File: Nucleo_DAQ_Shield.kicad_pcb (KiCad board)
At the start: 2 copper layers, 53.3 x 78.1 mm, 35 parts, among them J1 CONN_01X06, J2 CONN_01X06, J3 CONN_01X02, J4 CONN_01X02, J6 CONN_COAXIAL, J7 CONN_01X02, U1 4050, U10 ST_Nucleo144_F746ZG_CN10, U2 TL072, U3 LM7805CT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

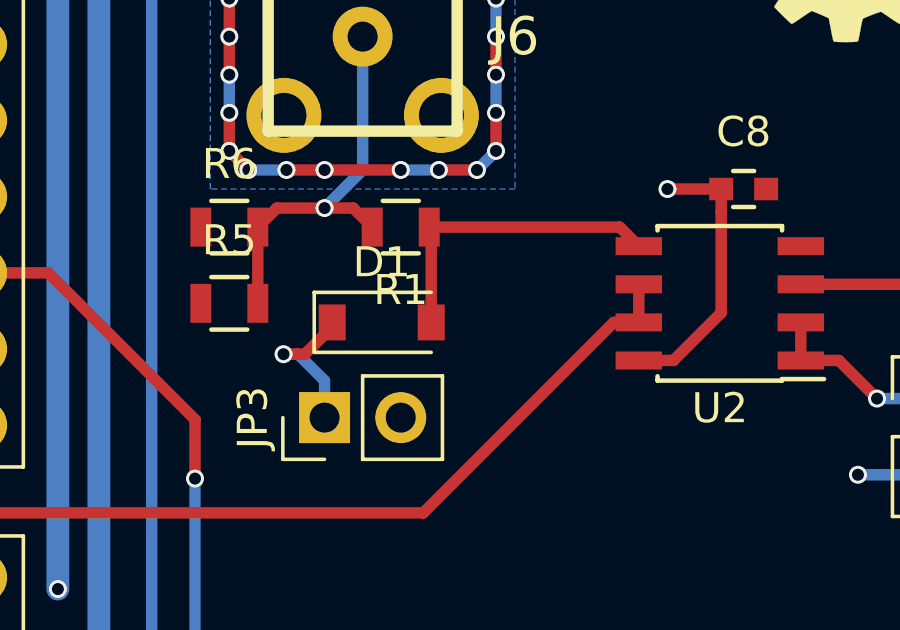
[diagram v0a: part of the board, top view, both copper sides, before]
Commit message: Added through hold Schottky diode as an alternative to SOD-123 Schottky diode
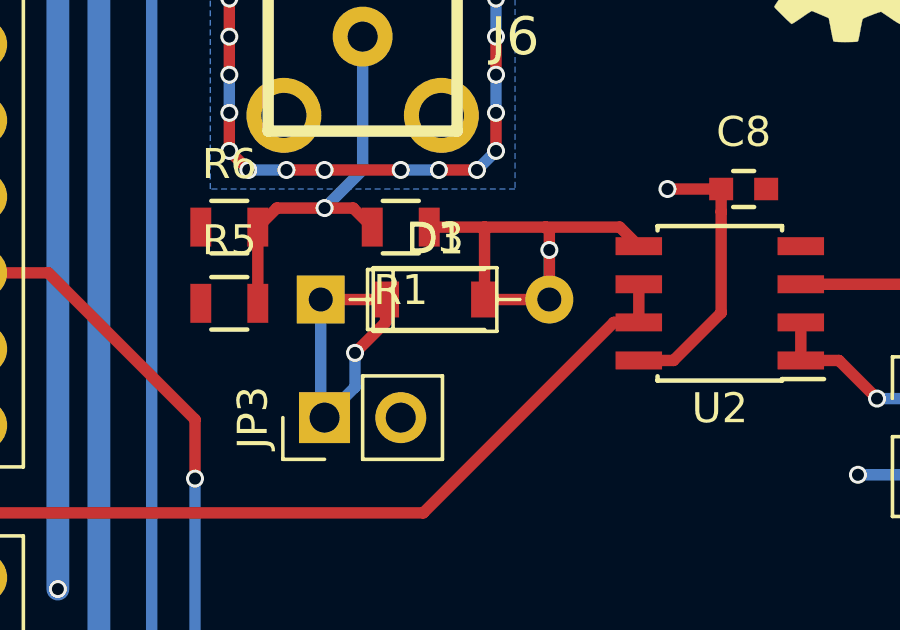
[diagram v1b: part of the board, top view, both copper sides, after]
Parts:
- added D3: SD103 DO-35, Diodes_THT:D_DO-35_SOD27_P7.62mm_Horizontal, F.Cu at (157.4, 79.9)
- D1: value D_Schottky -> SD103 SOD-123
- moved D1 1.94 mm to (161.2, 79.9)
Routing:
- net Net-(D1-Pad1): track 5.11 -> 10.9 mm
- net /ENVLP: track 10.4 -> 16.0 mm, vias 0 -> 1
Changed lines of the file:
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@@
 (kicad_pcb (version 4) (host pcbnew 4.0.6)
   (general
-    (links 0)
+    (links 79)
     (no_connects 2)
-    (area 140.894999 48.819999 194.385001 127.075001)
+    (area 133.708523 46.841 244.462898 140.391001)
     (thickness 1.6)
     (drawings 22)
-    (tracks 292)
+    (tracks 299)
     (zones 0)
-    (modules 35)
+    (modules 36)
     (nets 112)
   )
@@
     (visible_elements FFFFEF7F)
     (pcbplotparams
-      (layerselection 0x00030_80000001)
+      (layerselection 0x01000_80000001)
       (usegerberextensions false)
       (excludeedgelayer true)
@@
       (outputformat 1)
       (mirror false)
-      (drillshape 1)
+      (drillshape 0)
       (scaleselection 1)
-      (outputdirectory ""))
+      (outputdirectory gerbers/v1.0/))
   )
   (net 0 "")
@@
   )
   (module Diodes_SMD:D_SOD-123 (layer F.Cu)
-    (at 159.385 80.645)
+    (at 161.164 79.883)
     (descr SOD-123)
     (tags SOD-123)
@@
       (effects (font (size 1 1) (thickness 0.15)))
     )
-    (fp_text value D_Schottky (at 0 2.1) (layer F.Fab)
+    (fp_text value "SD103 SOD-123" (at 0 2.1) (layer F.Fab)
       (effects (font (size 1 1) (thickness 0.15)))
     )
@@
       (xy 0.500964 -3.601424)) (layer F.SilkS) (width 0.01))
   )
+  (module Diodes_THT:D_DO-35_SOD27_P7.62mm_Horizontal (layer F.Cu)
+    (at 157.353 79.883)
+    (descr "D, DO-35_SOD27 series, Axial, Horizontal, pin pitch=7.62mm, , length*diameter=4*2mm^2, , http://www.diodes.com/_files/packages/DO-35.pdf")
+    (tags "D DO-35_SOD27 series Axial Horizontal pin pitch 7.62mm  length 4mm diameter 2mm")
+    (fp_text reference D3 (at 3.81 -2.06) (layer F.SilkS)
+      (effects (font (size 1 1) (thickness 0.15)))
+    )
+    (fp_text value "SD103 DO-35" (at 3.81 2.06) (layer F.Fab)
+      (effects (font (size 1 1) (thickness 0.15)))
+    )
+    (fp_line (start 1.81 -1) (end 1.81 1) (layer F.Fab) (width 0.1))
+    (fp_line (start 1.81 1) (end 5.81 1) (layer F.Fab) (width 0.1))
+    (fp_line (start 5.81 1) (end 5.81 -1) (layer F.Fab) (width 0.1))
+    (fp_line (start 5.81 -1) (end 1.81 -1) (layer F.Fab) (width 0.1))
+    (fp_line (start 0 0) (end 1.81 0) (layer F.Fab) (width 0.1))
+    (fp_line (start 7.62 0) (end 5.81 0) (layer F.Fab) (width 0.1))
+    (fp_line (start 2.41 -1) (end 2.41 1) (layer F.Fab) (width 0.1))
+    (fp_line (start 1.75 -1.06) (end 1.75 1.06) (layer F.SilkS) (width 0.12))
+    (fp_line (start 1.75 1.06) (end 5.87 1.06) (layer F.SilkS) (width 0.12))
+    (fp_line (start 5.87 1.06) (end 5.87 -1.06) (layer F.SilkS) (width 0.12))
+    (fp_line (start 5.87 -1.06) (end 1.75 -1.06) (layer F.SilkS) (width 0.12))
+    (fp_line (start 0.98 0) (end 1.75 0) (layer F.SilkS) (width 0.12))
+    (fp_line (start 6.64 0) (end 5.87 0) (layer F.SilkS) (width 0.12))
+    (fp_line (start 2.41 -1.06) (end 2.41 1.06) (layer F.SilkS) (width 0.12))
+    (fp_line (start -1.05 -1.35) (end -1.05 1.35) (layer F.CrtYd) (width 0.05))
+    (fp_line (start -1.05 1.35) (end 8.7 1.35) (layer F.CrtYd) (width 0.05))
+    (fp_line (start 8.7 1.35) (end 8.7 -1.35) (layer F.CrtYd) (width 0.05))
+    (fp_line (start 8.7 -1.35) (end -1.05 -1.35) (layer F.CrtYd) (width 0.05))
+    (pad 1 thru_hole rect (at 0 0) (size 1.6 1.6) (drill 0.8) (layers *.Cu *.Mask)
+      (net 5 "Net-(D1-Pad1)"))
+    (pad 2 thru_hole oval (at 7.62 0) (size 1.6 1.6) (drill 0.8) (layers *.Cu *.Mask)
+      (net 6 /ENVLP))
+    (model Diodes_THT.3dshapes/D_DO-35_SOD27_P7.62mm_Horizontal.wrl
+      (at (xyz 0 0 0))
+      (scale (xyz 0.393701 0.393701 0.393701))
+      (rotate (xyz 0 0 0))
+    )
+  )
   (gr_text "Nucleo DAQ Shield\nColumbia University\nCreative Machines Lab" (at 164.465 104.267 90) (layer F.SilkS)
     (effects (font (size 1.5 1.5) (thickness 0.3)))
@@
   (segment (start 170.7 76.956) (end 170.7 76.2) (width 0.381) (layer F.Cu) (net 4))
   (segment (start 177.05 106) (end 177.005 106.045) (width 0.381) (layer F.Cu) (net 4))
-  (segment (start 156.536591 81.705199) (end 156.112327 81.705199) (width 0.381) (layer F.Cu) (net 5))
-  (segment (start 156.824801 81.705199) (end 156.536591 81.705199) (width 0.381) (layer F.Cu) (net 5))
-  (segment (start 157.735 80.795) (end 156.824801 81.705199) (width 0.381) (layer F.Cu) (net 5))
-  (segment (start 157.735 80.645) (end 157.735 80.795) (width 0.381) (layer F.Cu) (net 5))
-  (segment (start 157.48 82.589) (end 156.596199 81.705199) (width 0.381) (layer B.Cu) (net 5))
-  (segment (start 157.48 83.82) (end 157.48 82.589) (width 0.381) (layer B.Cu) (net 5))
-  (segment (start 156.596199 81.705199) (end 156.112327 81.705199) (width 0.381) (layer B.Cu) (net 5))
-  (via (at 156.112327 81.705199) (size 0.6) (drill 0.4) (layers F.Cu B.Cu) (net 5))
-  (segment (start 160.97 77.47) (end 167.32 77.47) (width 0.381) (layer F.Cu) (net 6))
+  (segment (start 158.496 81.661) (end 158.496 82.804) (width 0.381) (layer B.Cu) (net 5))
+  (segment (start 158.496 82.804) (end 157.48 83.82) (width 0.381) (layer B.Cu) (net 5))
+  (segment (start 159.514 79.883) (end 159.514 80.643) (width 0.381) (layer F.Cu) (net 5))
+  (segment (start 159.514 80.643) (end 158.496 81.661) (width 0.381) (layer F.Cu) (net 5))
+  (via (at 158.496 81.661) (size 0.6) (drill 0.4) (layers F.Cu B.Cu) (net 5))
+  (segment (start 157.353 79.883) (end 157.353 83.693) (width 0.381) (layer B.Cu) (net 5))
+  (segment (start 157.353 83.693) (end 157.48 83.82) (width 0.381) (layer B.Cu) (net 5))
+  (segment (start 159.514 79.883) (end 157.353 79.883) (width 0.381) (layer F.Cu) (net 5))
+  (segment (start 160.97 77.47) (end 162.814 77.47) (width 0.381) (layer F.Cu) (net 6))
+  (segment (start 162.814 77.47) (end 164.846 77.47) (width 0.381) (layer F.Cu) (net 6))
+  (segment (start 162.814 79.883) (end 162.814 77.47) (width 0.381) (layer F.Cu) (net 6))
+  (segment (start 164.973 79.883) (end 164.973 78.232) (width 0.381) (layer B.Cu) (net 6))
+  (via (at 164.973 78.232) (size 0.6) (drill 0.4) (layers F.Cu B.Cu) (net 6))
+  (segment (start 164.973 79.883) (end 162.814 79.883) (width 0.381) (layer F.Cu) (net 6))
+  (segment (start 164.846 77.47) (end 167.32 77.47) (width 0.381) (layer F.Cu) (net 6))
+  (segment (start 164.846 77.47) (end 164.973 77.597) (width 0.381) (layer F.Cu) (net 6))
+  (segment (start 164.973 77.597) (end 164.973 79.883) (width 0.381) (layer F.Cu) (net 6))
   (segment (start 167.32 77.47) (end 167.955 78.105) (width 0.381) (layer F.Cu) (net 6))
-  (segment (start 161.035 80.645) (end 161.035 77.535) (width 0.381) (layer F.Cu) (net 6))
   (segment (start 161.035 77.535) (end 160.97 77.47) (width 0.381) (layer F.Cu) (net 6))
   (segment (start 163.83 59.69) (end 163.195 59.69) (width 0.381) (layer B.Cu) (net 7))

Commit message: Nucleo DAQ Shield v1.2
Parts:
- U3: value LM7805CT -> L78L05
- U5: footprint Housings_SOIC:SOIC-8_3.9x4.9mm_Pitch1.27mm -> custom:SOIC-8_PowerPad
- moved R3 0.63 mm to (151.1, 114.9)
- moved U5 0.57 mm to (153.8, 110.1), turned to 270 degrees
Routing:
- net /MOTOR+: track 23.9 -> 19.9 mm
- net Vbat: track 88.9 -> 89.7 mm
- net Net-(R3-Pad1): track 2.68 -> 2.00 mm
- net /MOTOR_PWM_FORWARD: track 6.19 -> 5.67 mm

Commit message: Added stencil file with 7mil mask to paste clearance
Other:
- rule pad_to_mask_clearance: 0.2 -> 0
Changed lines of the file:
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@@
     (pad_size 1.524 1.524)
     (pad_drill 0.762)
-    (pad_to_mask_clearance 0.2)
+    (pad_to_mask_clearance 0)
+    (pad_to_paste_clearance -0.0762)
     (aux_axis_origin 0 0)
     (visible_elements FFFFEF7F)
     (pcbplotparams
-      (layerselection 0x01000_80000001)
+      (layerselection 0x01008_80000001)
       (usegerberextensions false)
       (excludeedgelayer true)
@@
       (drillshape 0)
       (scaleselection 1)
-      (outputdirectory gerbers/v1.0/))
+      (outputdirectory gerbers/v1.2/))
   )
   (net 0 "")
